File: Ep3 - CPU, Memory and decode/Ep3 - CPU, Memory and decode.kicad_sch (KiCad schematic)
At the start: 23 parts, among them J1 +5V DC, SW1 POWER SW, SW2 RST SW, U1 74HCT20, U2 74HCT14, U3 74HCT112, U4 74HCT74, X1 4MHz

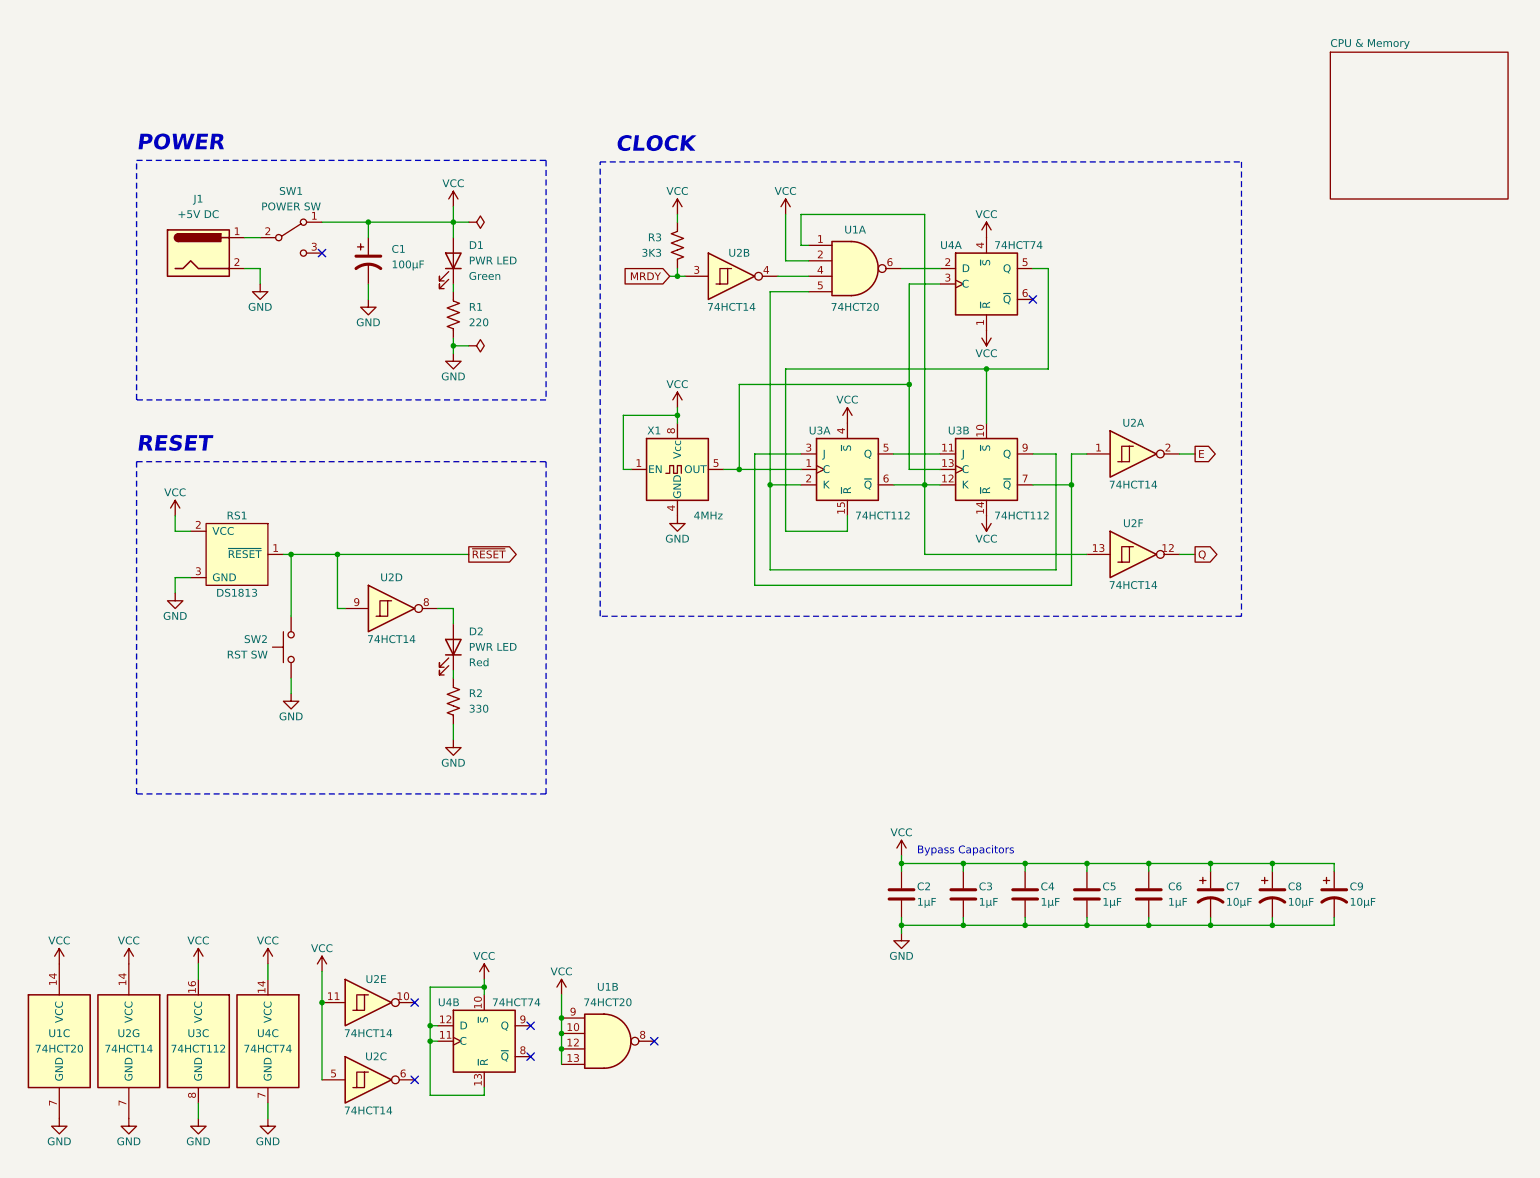
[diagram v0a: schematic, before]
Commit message: Minor cosmetic changes
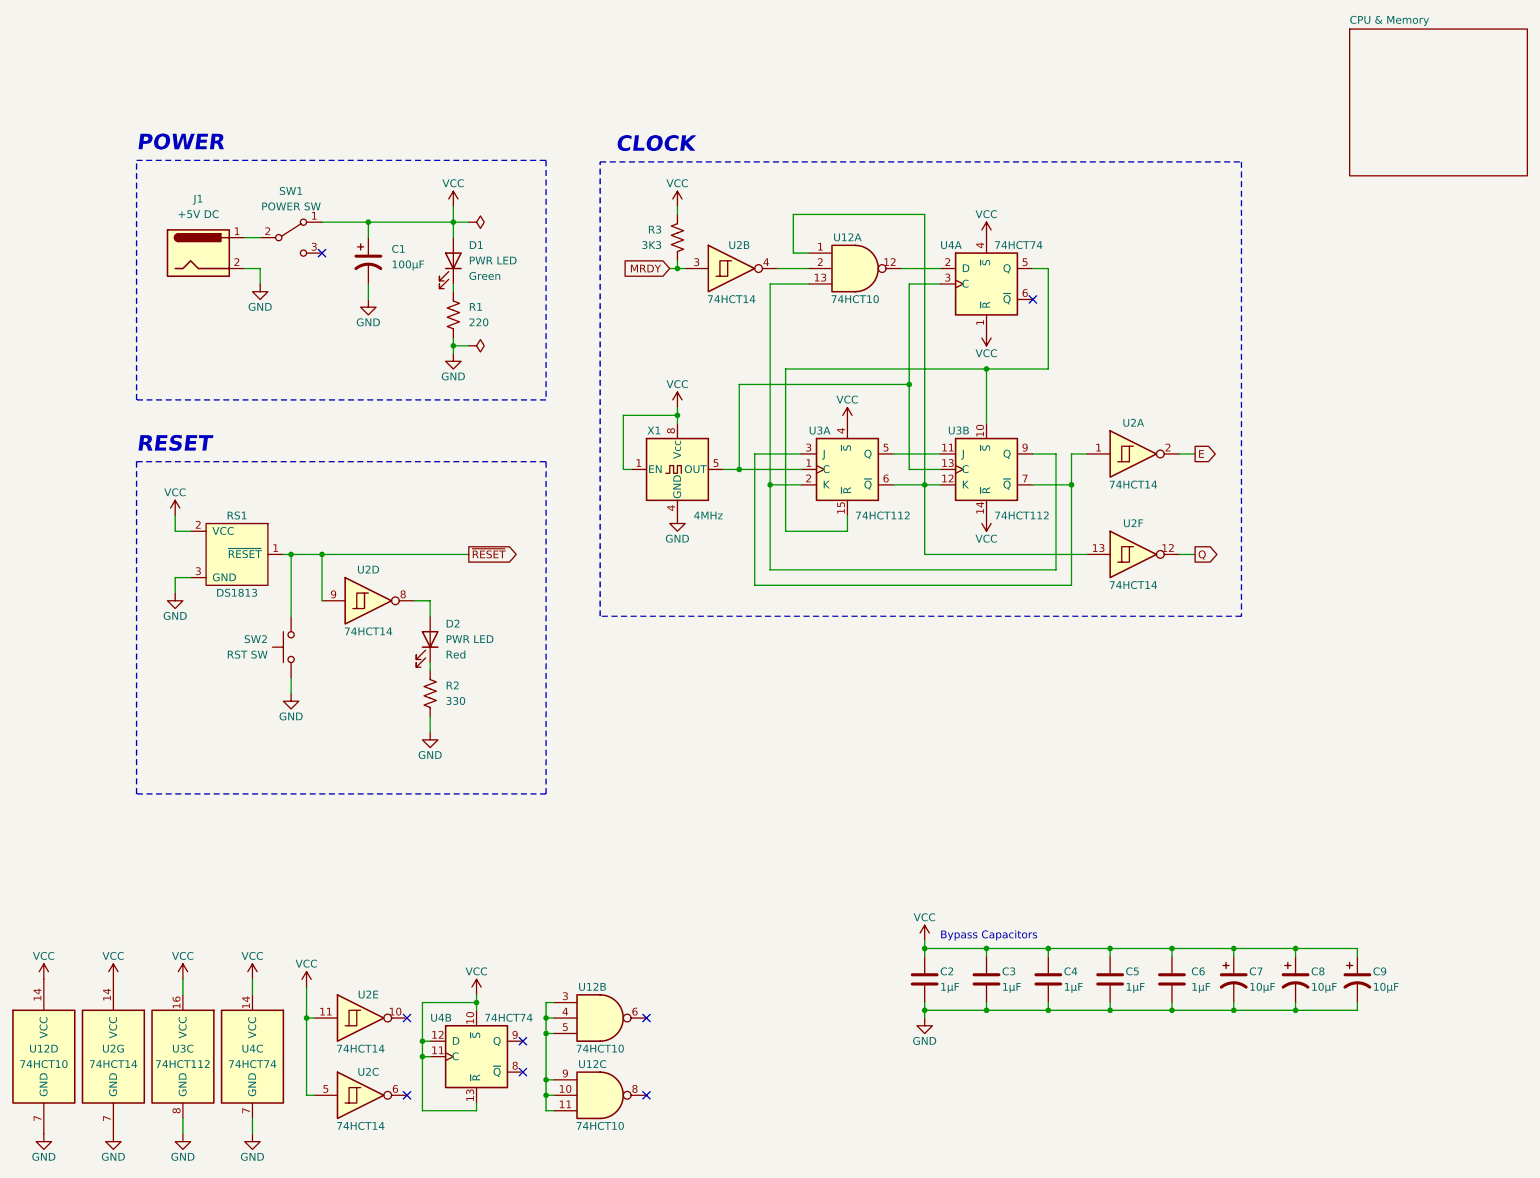
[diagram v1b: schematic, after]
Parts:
- removed U1: 74HCT20, symbol 74xx:74LS20
- added U12: 74HCT10, symbol 74xx:74LS10
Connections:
- net GND: now also U12.7 (GND)
- net VCC: now also U12.14 (VCC)
- net at U4.2 (D): now also U12.12
- net at U2.13, U3.12 (K), U3.6 (~{Q}): now also U12.1
- net at U2.4: now also U12.2
- net at U3.2 (K), U3.9 (Q): now also U12.13
- new net: U12.10, U12.11, U12.3, U12.4, U12.5, U12.9
- no-connect marks 7 -> 8
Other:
- title: Power, Reset, Clock, and CPU NOP test circuit -> Power, Reset, Clock
- moved on the sheet: C2, C3, C4, C5, C6, C7, C8, C9, D2, R2, R3, U2B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
